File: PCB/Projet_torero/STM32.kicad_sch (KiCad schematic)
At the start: 0 parts

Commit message: Rajouté la STM32
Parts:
- added C1, C2: C_Small, symbol Device:C_Small
- added C10, C9: 1µF, symbol Device:C_Small
- added C11, C4, C5, C6: 100nF, symbol Device:C_Small
- added C3: 0.1 pF, symbol Device:C_Small
- added C7: 4.7nF, symbol Device:C_Small
- added C8: 10nF, symbol Device:C_Small
- added R1, R2: R_Small, symbol Device:R_Small
- added SW1, SW2: SW_Push, symbol Switch:SW_Push
- added U1: STM32G431CBUx, Package_DFN_QFN:QFN-48-1EP_7x7mm_P0.5mm_EP5.6x5.6mm, symbol MCU_ST_STM32G4:STM32G431CBUx
- added Y1: Crystal_GND24_Small, symbol Device:Crystal_GND24_Small
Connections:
- new net: C2.2, R1.2, Y1.1
- new net: C8.1, C9.1, U1.21 (VDDA)
- new net: C4.2, C5.2, C6.2, C7.2, U1.23 (VDD), U1.35 (VDD), U1.48 (VDD)
- new net: R1.1, U1.4 (PC15)
- new net: C1.2, U1.3 (PC14), Y1.3
- new net: R2.2, SW1.1, U1.46 (PB8)
- new net: C3.1, SW2.2, U1.7 (PG10)
- new net +3.3V: C4.1, C5.1, C6.1, C7.1, SW1.2, U1.1 (VBAT)
- new net GND: C1.1, C10.2, C11.2, C2.1, C3.2, C8.2, C9.2, R2.1, SW2.1, U1.49 (VSS), Y1.2, Y1.4
- new net V_Ref: C10.1, C11.1, U1.20 (VREF+)
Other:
- note added: "BOOT_Flash"
- note added: "Reset"

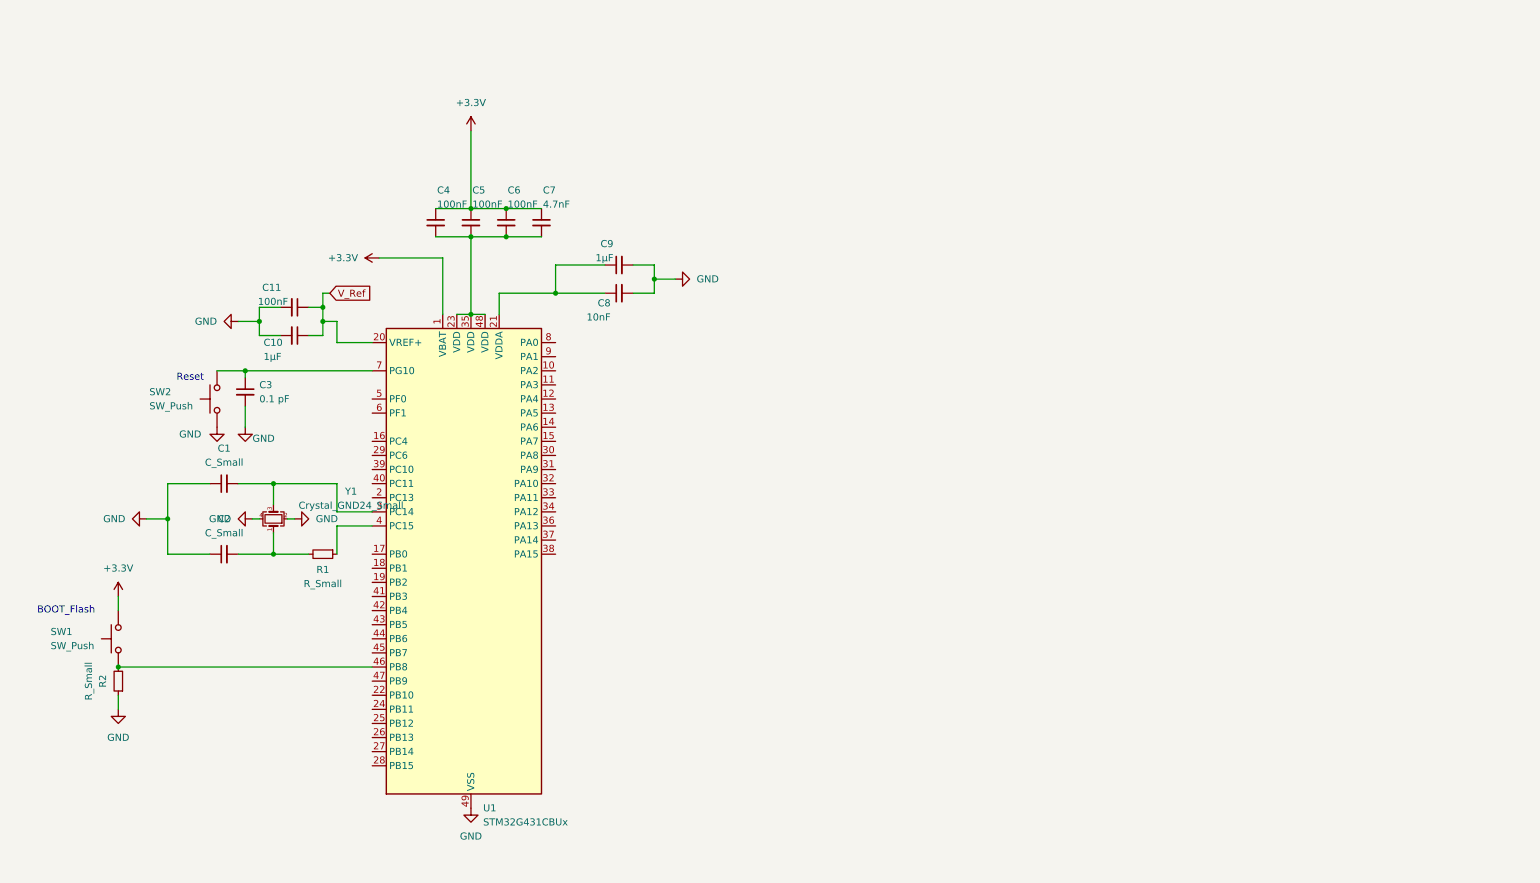
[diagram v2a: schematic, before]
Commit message: Rajouté la STM32
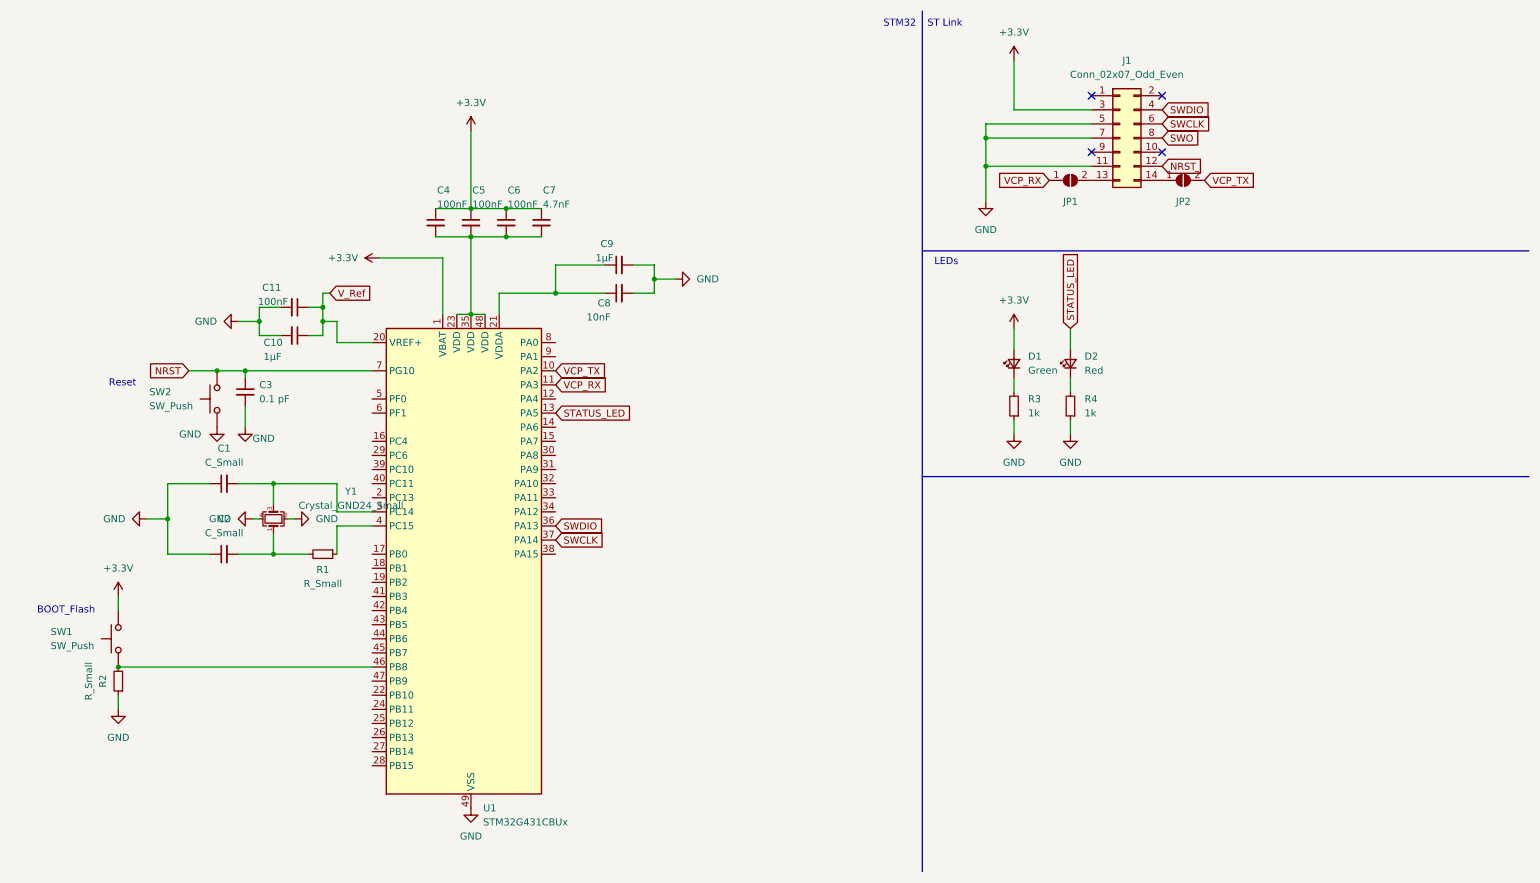
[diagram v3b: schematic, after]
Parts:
- added D1: Green, LED_SMD:LED_0603_1608Metric_Pad1.05x0.95mm_HandSolder, symbol Device:LED_Small
- added D2: Red, LED_SMD:LED_0603_1608Metric_Pad1.05x0.95mm_HandSolder, symbol Device:LED_Small
- added J1: Conn_02x07_Odd_Even, symbol Connector_Generic:Conn_02x07_Odd_Even
- added JP1, JP2: SolderJumper_2_Open, Jumper:SolderJumper-2_P1.3mm_Open_TrianglePad1.0x1.5mm, symbol Jumper:SolderJumper_2_Open
- added R3, R4: 1k, Resistor_SMD:R_0603_1608Metric_Pad0.98x0.95mm_HandSolder, symbol Device:R_Small
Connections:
- net +3.3V: now also D1.2 (A), J1.3 (Pin_3)
- net GND: now also J1.11 (Pin_11), J1.5 (Pin_5), J1.7 (Pin_7), R3.1, R4.1
- net VCP_TX: now reaches U1.10 (PA2)
- net VCP_TX: now also JP2.2 (B)
- net VCP_RX: now reaches U1.11 (PA3)
- net VCP_RX: now also JP1.1 (A)
- net STATUS_LED: now reaches U1.13 (PA5)
- net STATUS_LED: now also D2.2 (A)
- net SWDIO: now reaches U1.36 (PA13)
- net SWDIO: now also J1.4 (Pin_4)
- net SWCLK: now reaches U1.37 (PA14)
- net SWCLK: now also J1.6 (Pin_6)
- net NRST: now reaches C3.1, SW2.2, U1.7 (PG10)
- net NRST: now also J1.12 (Pin_12)
- new net: J1.13 (Pin_13), JP1.2 (B)
- new net: J1.14 (Pin_14), JP2.1 (A)
- new net: D1.1 (K), R3.2
- new net: D2.1 (K), R4.2
- new net SWO: J1.8 (Pin_8)
- no-connect marks 0 -> 4
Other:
- note added: "LEDs"
- note added: "ST Link"
- note added: "STM32"

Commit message: Add files via upload
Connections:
- net STATUS_LED: now also U1.34 (PA12); no longer U1.13 (PA5)
- net CS: now reaches U1.12 (PA4)
- net SDO/ADDR: now reaches U1.14 (PA6)
- net SDA/SDI/SDIO: now reaches U1.15 (PA7)
- net ANALOG_OUTPUT_1: now reaches U1.17 (PB0)
- net ANALOG_OUTPUT_2: now reaches U1.18 (PB1)
- net M_EN: now reaches U1.19 (PB2)
- net Rx: now reaches U1.22 (PB10)
- net Tx: now reaches U1.24 (PB11)
- net FWDG: now reaches U1.30 (PA8)
- net REVG: now reaches U1.31 (PA9)
- net INT1: now reaches U1.32 (PA10)
- net INT2: now reaches U1.33 (PA11)
- net DEV_EN: now reaches U1.41 (PB3)
- net M_SCTR: now reaches U1.42 (PB4)
- net FWDD: now reaches U1.8 (PA0)
- net REVD: now reaches U1.9 (PA1)
- new net SCLK: U1.13 (PA5)
- no-connect marks 4 -> 20
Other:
- moved on the sheet: C1, C2, R1, Y1

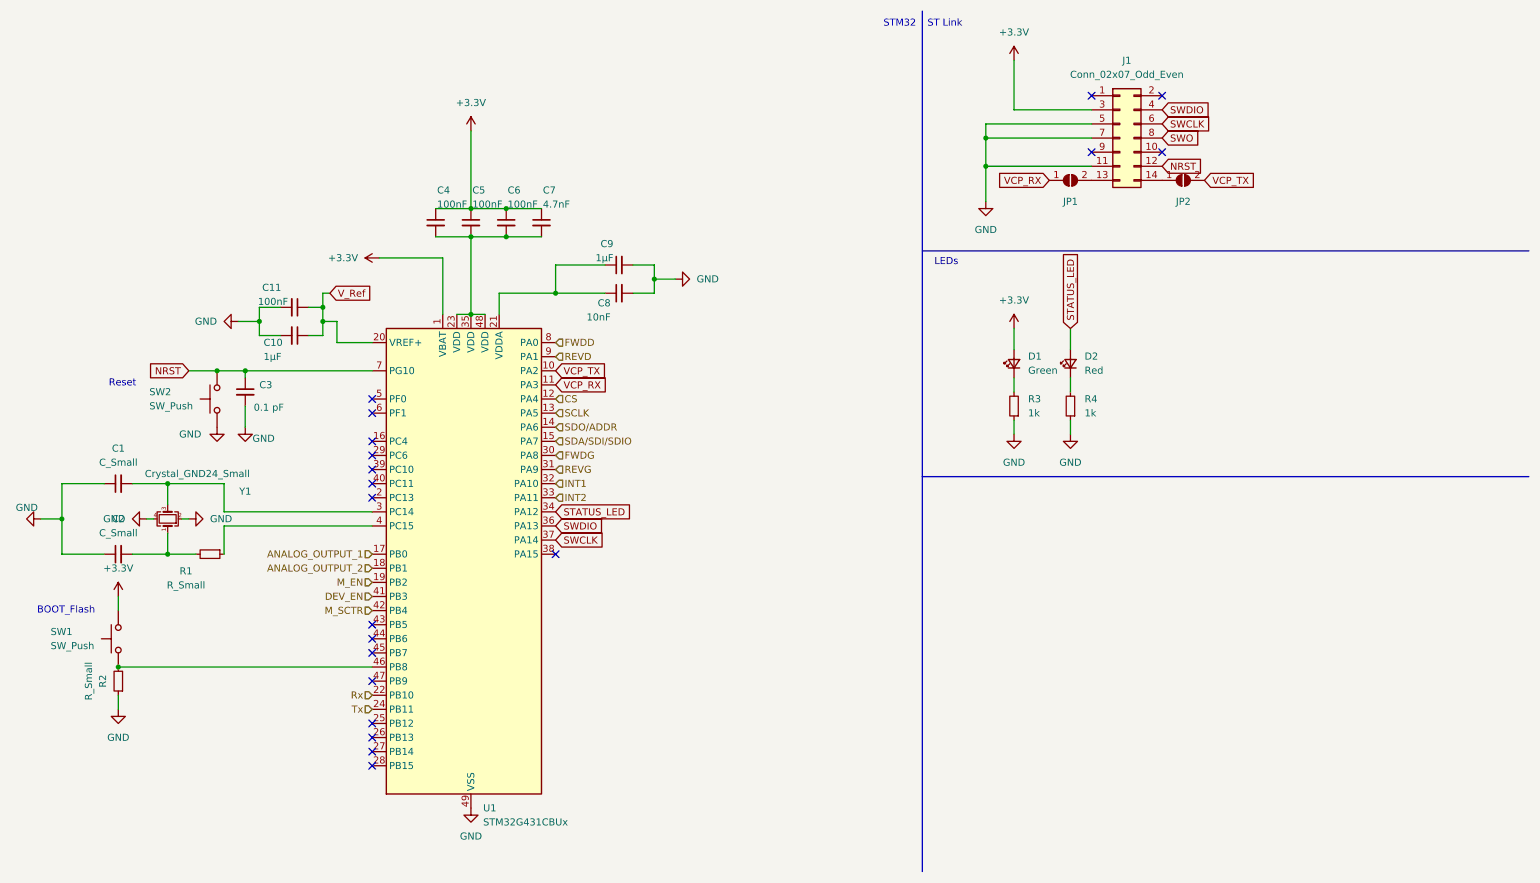
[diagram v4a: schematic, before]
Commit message: Corriger les erreurs de la STM
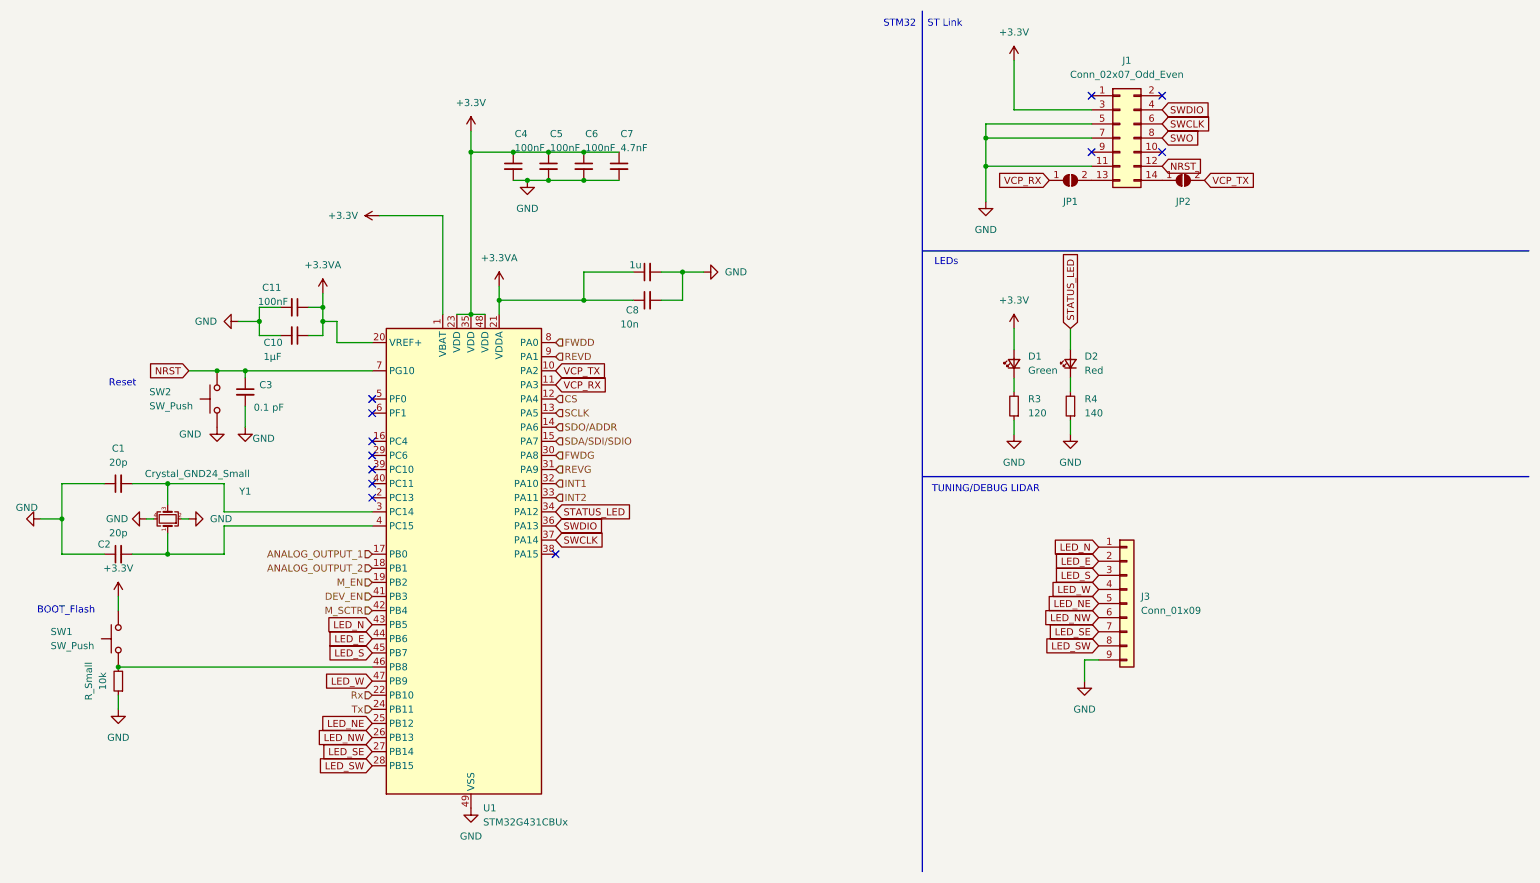
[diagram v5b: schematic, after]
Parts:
- removed R1: R_Small, symbol Device:R_Small
- added J3: Conn_01x09, symbol Connector_Generic:Conn_01x09
- C1, C2: value C_Small -> 20p
- C8: value 10nF -> 10n
- C9: value 1µF -> 1u
- R3: value 1k -> 120
- R4: value 1k -> 140
- renumbered R2 to 10k
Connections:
- net V_Ref is gone; now on net +3.3VA: C10.1, C11.1, U1.20 (VREF+)
- net +3.3V: now also U1.23 (VDD), U1.35 (VDD), U1.48 (VDD)
- net GND: now also C4.2, C5.2, C6.2, C7.2, J3.9 (Pin_9)
- net at C2.2, Y1.1: now also U1.4 (PC15)
- net +3.3VA: now reaches C8.1, C9.1, U1.21 (VDDA)
- net LED_NE: now reaches U1.25 (PB12)
- net LED_NE: now also J3.5 (Pin_5)
- net LED_NW: now reaches U1.26 (PB13)
- net LED_NW: now also J3.6 (Pin_6)
- net LED_SE: now reaches U1.27 (PB14)
- net LED_SE: now also J3.7 (Pin_7)
- net LED_SW: now reaches U1.28 (PB15)
- net LED_SW: now also J3.8 (Pin_8)
- net LED_N: now reaches U1.43 (PB5)
- net LED_N: now also J3.1 (Pin_1)
- net LED_E: now reaches U1.44 (PB6)
- net LED_E: now also J3.2 (Pin_2)
- net LED_S: now reaches U1.45 (PB7)
- net LED_S: now also J3.3 (Pin_3)
- net LED_W: now reaches U1.47 (PB9)
- net LED_W: now also J3.4 (Pin_4)
- no-connect marks 20 -> 12
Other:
- note added: "TUNING/DEBUG LIDAR"
- moved on the sheet: C8

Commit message: modif valeur composants passifs
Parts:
- C11, C4, C5, C6: value 100nF -> 100n
- C3: value 0.1 pF -> 0.1 p
- C7: value 4.7nF -> 4.7n
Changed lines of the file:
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@@
 			)
 		)
-		(property "Value" "100nF"
+		(property "Value" "100n"
 			(at 115.824 36.068 0)
 			(effects
@@
 			)
 		)
-		(property "Value" "100nF"
+		(property "Value" "100n"
 			(at 109.474 36.068 0)
 			(effects
@@
 			)
 		)
-		(property "Value" "4.7nF"
+		(property "Value" "4.7n"
 			(at 122.174 36.068 0)
 			(effects
@@
 			)
 		)
-		(property "Value" "0.1 pF"
+		(property "Value" "0.1 p"
 			(at 56.134 82.804 0)
 			(effects
@@
 			)
 		)
-		(property "Value" "100nF"
+		(property "Value" "100n"
 			(at 103.124 36.068 0)
 			(effects
@@
 			)
 		)
-		(property "Value" "100nF"
+		(property "Value" "100n"
 			(at 56.896 63.754 90)
 			(effects

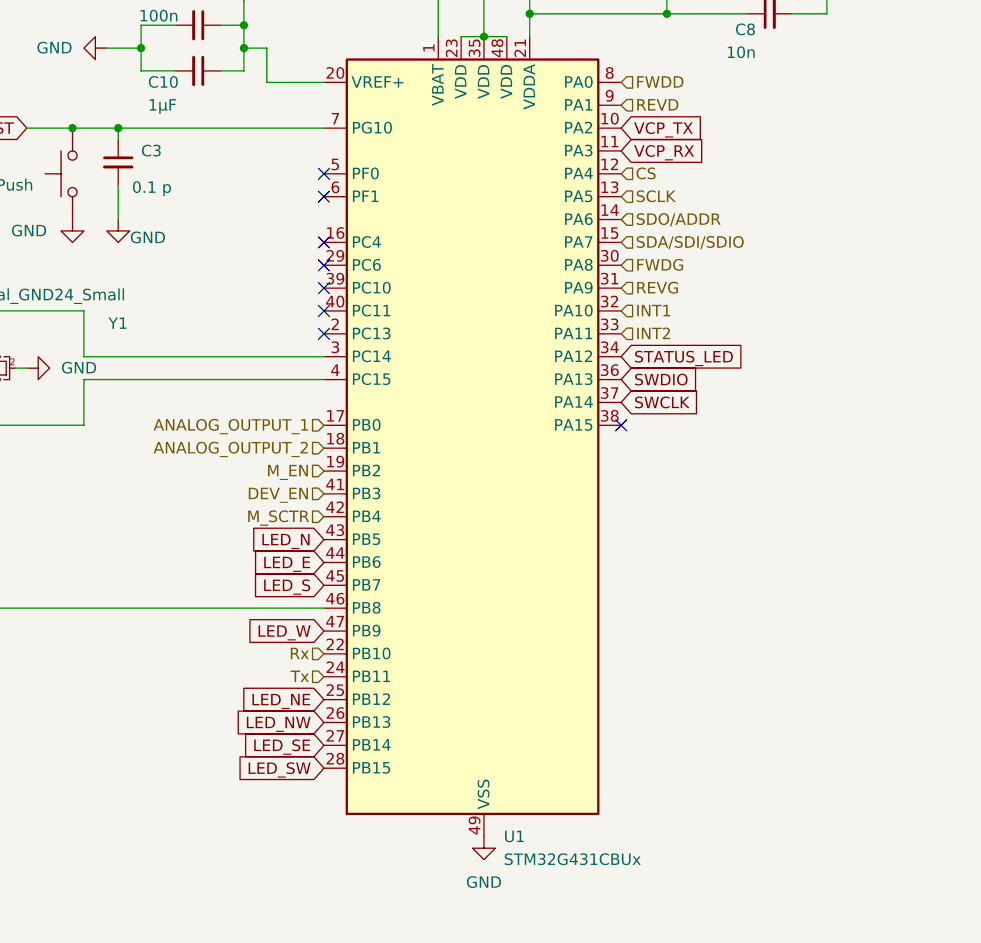
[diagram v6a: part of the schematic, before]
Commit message: Mit à jour les encodeurs
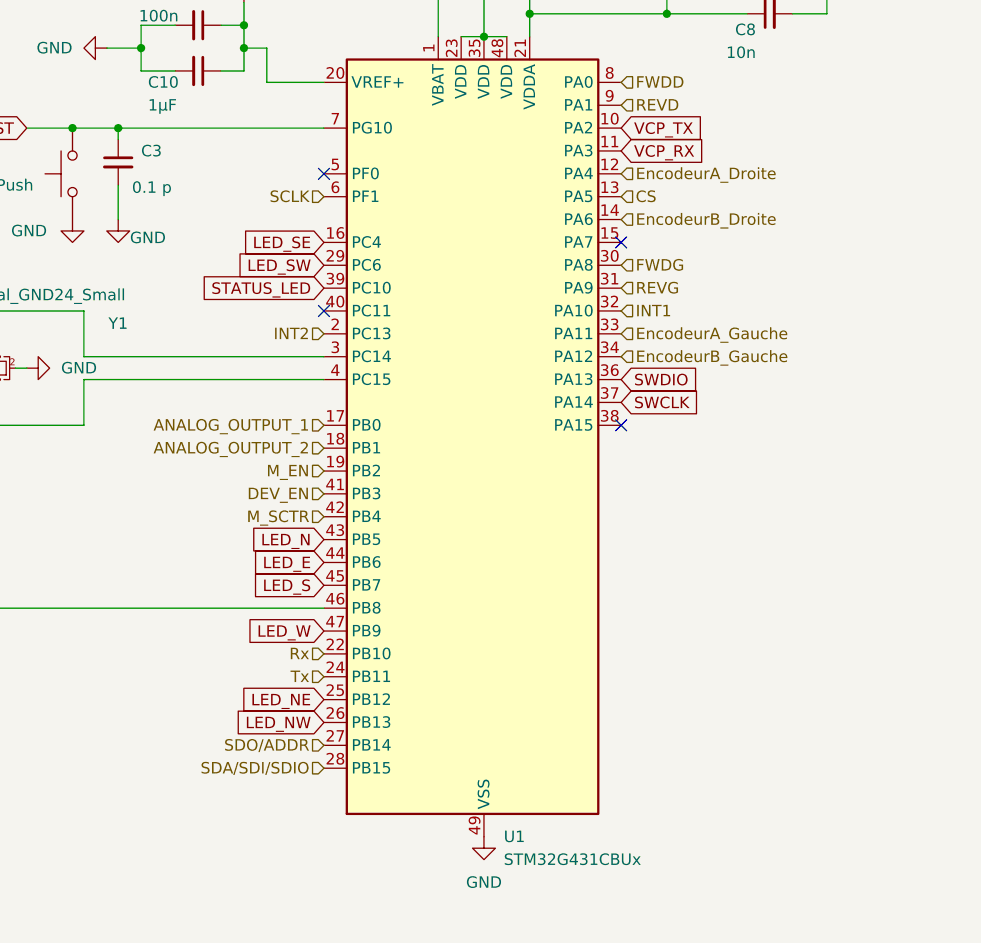
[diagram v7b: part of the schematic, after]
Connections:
- net CS: now also U1.13 (PA5); no longer U1.12 (PA4)
- net INT2: now also U1.2 (PC13); no longer U1.33 (PA11)
- net LED_SE: now also U1.16 (PC4); no longer U1.27 (PB14)
- net LED_SW: now also U1.29 (PC6); no longer U1.28 (PB15)
- net SCLK: now also U1.6 (PF1); no longer U1.13 (PA5)
- net SDA/SDI/SDIO: now also U1.28 (PB15); no longer U1.15 (PA7)
- net SDO/ADDR: now also U1.27 (PB14); no longer U1.14 (PA6)
- net STATUS_LED: now also U1.39 (PC10); no longer U1.34 (PA12)
- new net EncodeurA_Droite: U1.12 (PA4)
- new net EncodeurA_Gauche: U1.33 (PA11)
- new net EncodeurB_Droite: U1.14 (PA6)
- new net EncodeurB_Gauche: U1.34 (PA12)
- no-connect marks 12 -> 8
